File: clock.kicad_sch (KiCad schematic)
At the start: 39 parts, among them P16 SMA, P2 SMA, U19 SI5351C, U30 74LVC1G3157, U31 74LVC1G3157, U33 74HC4051, X1 TCXO

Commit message: Standardize component Value fields
Use Tolerance field instead of expressing tolerance in Value field
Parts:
- C113, C119, C120, C121, C122, C168, C39, C40, C43: value 1uF -> 1 uF
- C155: value 100nF -> 100 nF
- R27, R28: value 1k8 -> 1.8k
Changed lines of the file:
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@@
 			)
 		)
-		(property "Value" "1uF"
+		(property "Value" "1 uF"
 			(at 137.16 182.8799 0)
 			(effects
@@
 			)
 		)
-		(property "Value" "100nF"
+		(property "Value" "100 nF"
 			(at 88.9 99.06 90)
 			(effects
@@
 			)
 		)
-		(property "Value" "1uF"
+		(property "Value" "1 uF"
 			(at 124.46 182.8799 0)
 			(effects
@@
 			)
 		)
-		(property "Value" "1uF"
+		(property "Value" "1 uF"
 			(at 60.96 182.8799 0)
 			(effects
@@
 			)
 		)
-		(property "Value" "1uF"
+		(property "Value" "1 uF"
 			(at 99.06 182.8799 0)
 			(effects
@@
 			)
 		)
-		(property "Value" "1uF"
+		(property "Value" "1 uF"
 			(at 111.76 182.8799 0)
 			(effects
@@
 			)
 		)
-		(property "Value" "1uF"
+		(property "Value" "1 uF"
 			(at 149.86 182.8799 0)
 			(effects
@@
 			)
 		)
-		(property "Value" "1uF"
+		(property "Value" "1 uF"
 			(at 86.36 182.8799 0)
 			(effects
@@
 			)
 		)
-		(property "Value" "1k8"
+		(property "Value" "1.8k"
 			(at 63.5 139.6999 0)
 			(effects
@@
 			)
 		)
-		(property "Value" "1uF"
+		(property "Value" "1 uF"
 			(at 163.83 182.8799 0)
 			(effects
@@
 			)
 		)
-		(property "Value" "1uF"
+		(property "Value" "1 uF"
 			(at 73.66 182.8799 0)
 			(effects
@@
 			)
 		)
-		(property "Value" "1k8"
+		(property "Value" "1.8k"
 			(at 53.34 139.6999 0)
 			(effects

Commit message: Tune mixer output bias and balun
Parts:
- R108, R12, R23, R31, R32, R34, R41, R84: footprint Resistor_SMD:R_0402_1005Metric -> Resistor_SMD:R_0201_0603Metric; Part Number RC0402JR-0733RL -> RC0201JR-0733RL
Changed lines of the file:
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@@
 			)
 		)
-		(property "Footprint" "Resistor_SMD:R_0402_1005Metric"
+		(property "Footprint" "Resistor_SMD:R_0201_0603Metric"
 			(at 152.4 160.02 0)
 			(effects
@@
 			)
 		)
-		(property "Description" "RES 33 OHM 5% 1/16W 0402"
+		(property "Description" "RES 33 OHM 5% 1/20W 0201"
 			(at 152.4 160.02 0)
 			(effects
@@
 			)
 		)
-		(property "Part Number" "RC0402JR-0733RL"
+		(property "Part Number" "RC0201JR-0733RL"
 			(at 152.4 160.02 0)
 			(effects
@@
 			)
 		)
-		(property "Footprint" "Resistor_SMD:R_0402_1005Metric"
+		(property "Footprint" "Resistor_SMD:R_0201_0603Metric"
 			(at 152.4 109.22 0)
 			(effects
@@
 			)
 		)
-		(property "Description" "RES 33 OHM 5% 1/16W 0402"
+		(property "Description" "RES 33 OHM 5% 1/20W 0201"
 			(at 152.4 109.22 0)
 			(effects
@@
 			)
 		)
-		(property "Part Number" "RC0402JR-0733RL"
+		(property "Part Number" "RC0201JR-0733RL"
 			(at 152.4 109.22 0)
 			(effects
@@
 			)
 		)
-		(property "Footprint" "Resistor_SMD:R_0402_1005Metric"
+		(property "Footprint" "Resistor_SMD:R_0201_0603Metric"
 			(at 152.4 88.9 0)
 			(effects
@@
 			)
 		)
-		(property "Description" "RES 33 OHM 5% 1/16W 0402"
+		(property "Description" "RES 33 OHM 5% 1/20W 0201"
 			(at 152.4 88.9 0)
 			(effects
@@
 			)
 		)
-		(property "Part Number" "RC0402JR-0733RL"
+		(property "Part Number" "RC0201JR-0733RL"
 			(at 152.4 88.9 0)
 			(effects
@@
 			)
 		)
-		(property "Footprint" "Resistor_SMD:R_0402_1005Metric"
+		(property "Footprint" "Resistor_SMD:R_0201_0603Metric"
 			(at 152.4 129.54 0)
 			(effects
@@
 			)
 		)
-		(property "Description" "RES 33 OHM 5% 1/16W 0402"
+		(property "Description" "RES 33 OHM 5% 1/20W 0201"
 			(at 152.4 129.54 0)
 			(effects
@@
 			)
 		)
-		(property "Part Number" "RC0402JR-0733RL"
+		(property "Part Number" "RC0201JR-0733RL"
 			(at 152.4 129.54 0)
 			(effects
@@
 			)
 		)
-		(property "Footprint" "Resistor_SMD:R_0402_1005Metric"
+		(property "Footprint" "Resistor_SMD:R_0201_0603Metric"
 			(at 152.4 139.7 0)
 			(effects
@@
 			)
 		)
-		(property "Description" "RES 33 OHM 5% 1/16W 0402"
+		(property "Description" "RES 33 OHM 5% 1/20W 0201"
 			(at 152.4 139.7 0)
 			(effects
@@
 			)
 		)
-		(property "Part Number" "RC0402JR-0733RL"
+		(property "Part Number" "RC0201JR-0733RL"
 			(at 152.4 139.7 0)
 			(effects
@@
 			)
 		)
-		(property "Footprint" "Resistor_SMD:R_0402_1005Metric"
+		(property "Footprint" "Resistor_SMD:R_0201_0603Metric"
 			(at 152.4 99.06 0)
 			(effects
@@
 			)
 		)
-		(property "Description" "RES 33 OHM 5% 1/16W 0402"
+		(property "Description" "RES 33 OHM 5% 1/20W 0201"
 			(at 152.4 99.06 0)
 			(effects
@@
 			)
 		)
-		(property "Part Number" "RC0402JR-0733RL"
+		(property "Part Number" "RC0201JR-0733RL"
 			(at 152.4 99.06 0)
 			(effects
@@
 			)
 		)
-		(property "Footprint" "Resistor_SMD:R_0402_1005Metric"
+		(property "Footprint" "Resistor_SMD:R_0201_0603Metric"
 			(at 232.41 99.06 0)
 			(effects
@@
 			)
 		)
-		(property "Description" "RES 33 OHM 5% 1/16W 0402"
+		(property "Description" "RES 33 OHM 5% 1/20W 0201"
 			(at 232.41 99.06 0)
 			(effects
@@
 			)
 		)
-		(property "Part Number" "RC0402JR-0733RL"
+		(property "Part Number" "RC0201JR-0733RL"
 			(at 232.41 99.06 0)
 			(effects
@@
 			)
 		)
-		(property "Footprint" "Resistor_SMD:R_0402_1005Metric"
+		(property "Footprint" "Resistor_SMD:R_0201_0603Metric"
 			(at 152.4 149.86 0)
 			(effects
@@
 			)
 		)
-		(property "Description" "RES 33 OHM 5% 1/16W 0402"
+		(property "Description" "RES 33 OHM 5% 1/20W 0201"
 			(at 152.4 149.86 0)
 			(effects
@@
 			)
 		)
-		(property "Part Number" "RC0402JR-0733RL"
+		(property "Part Number" "RC0201JR-0733RL"
 			(at 152.4 149.86 0)
 			(effects

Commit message: Connect trigger and PPS I/O signals to MCU
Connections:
- net P6_3 renamed P2_5
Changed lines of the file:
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@@
+		)
+	)
+	(hierarchical_label "P2_5"
+		(shape bidirectional)
+		(at 97.79 69.85 0)
+		(effects
+			(font
+				(size 1.524 1.524)
+			)
+			(justify left)
 		)
 	)
@@
 		)
 	)
-	(hierarchical_label "P6_3"
-		(shape bidirectional)
-		(at 97.79 69.85 0)
-		(effects
-			(font
-				(size 1.524 1.524)
-			)
-			(justify left)
-		)
-	)

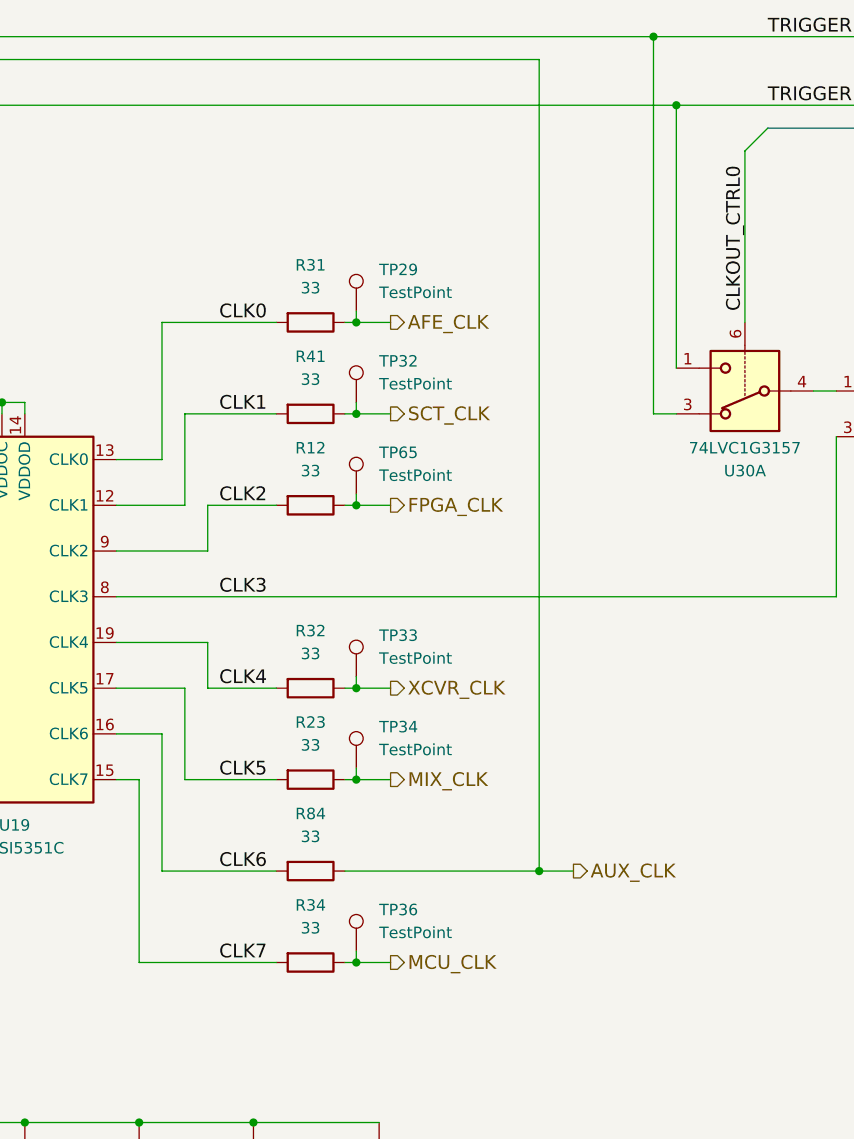
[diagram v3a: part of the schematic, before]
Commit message: Move MCU_CLK from CLK7 to CLK2
- Move FPGA_CLK from CLK2 to CLK1, shared with SCT_CLK
- Add AUX_CLK2 on CLK7
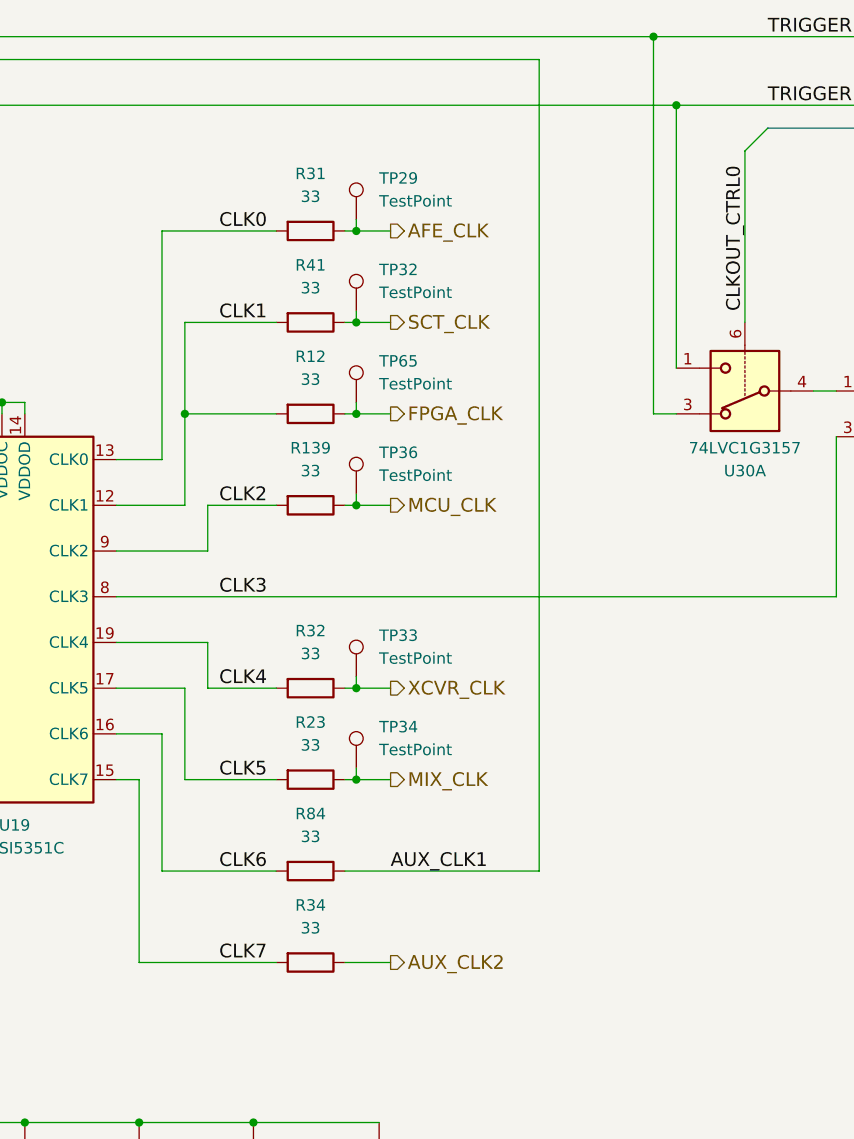
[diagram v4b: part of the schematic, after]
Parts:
- added R139: 33, Resistor_SMD:R_0201_0603Metric, symbol Device:R
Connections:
- net CLK1: now also R12.2
- net CLK2: now also R139.2; no longer R12.2
- net MCU_CLK: now also R139.1; no longer R34.1
- net AUX_CLK renamed AUX_CLK1
- new net AUX_CLK2: R34.1
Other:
- moved on the sheet: R12, R31, R41, TP29, TP32, TP36, TP65

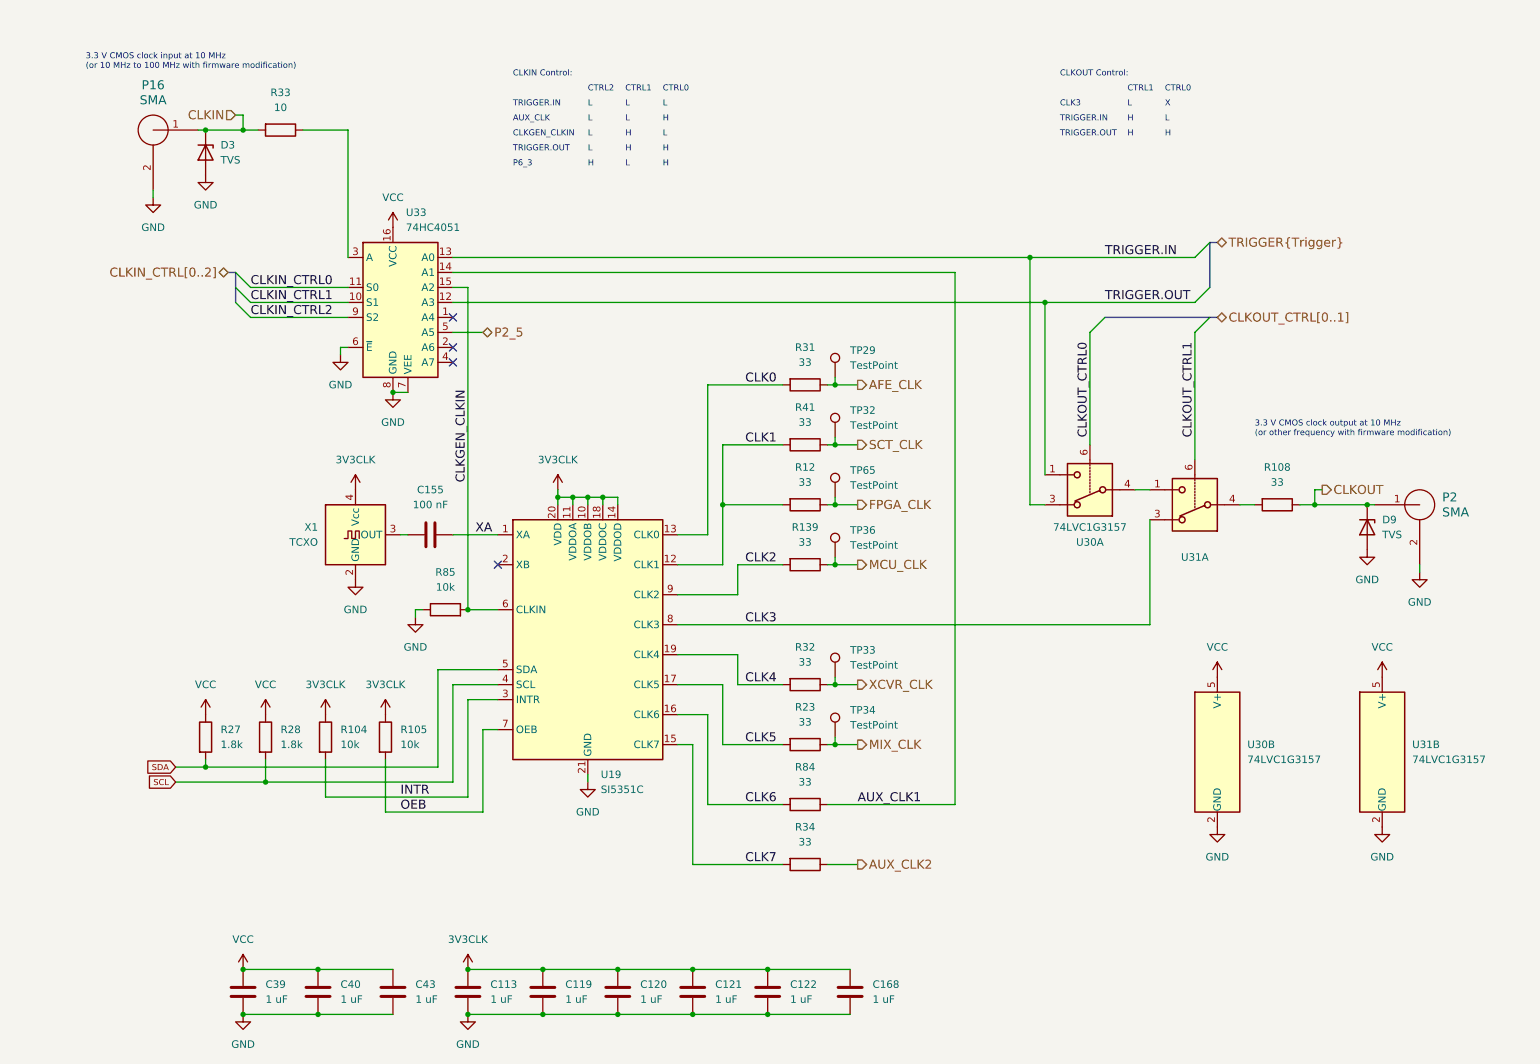
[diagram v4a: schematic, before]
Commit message: Add CLKIN selector switch
- Rename CLKIN SMA connector to P1
- Rename CLKOUT SMA connector to P2
- Allow selection of CLKIN from either P1 or P22
- Add more signals to P1 mux
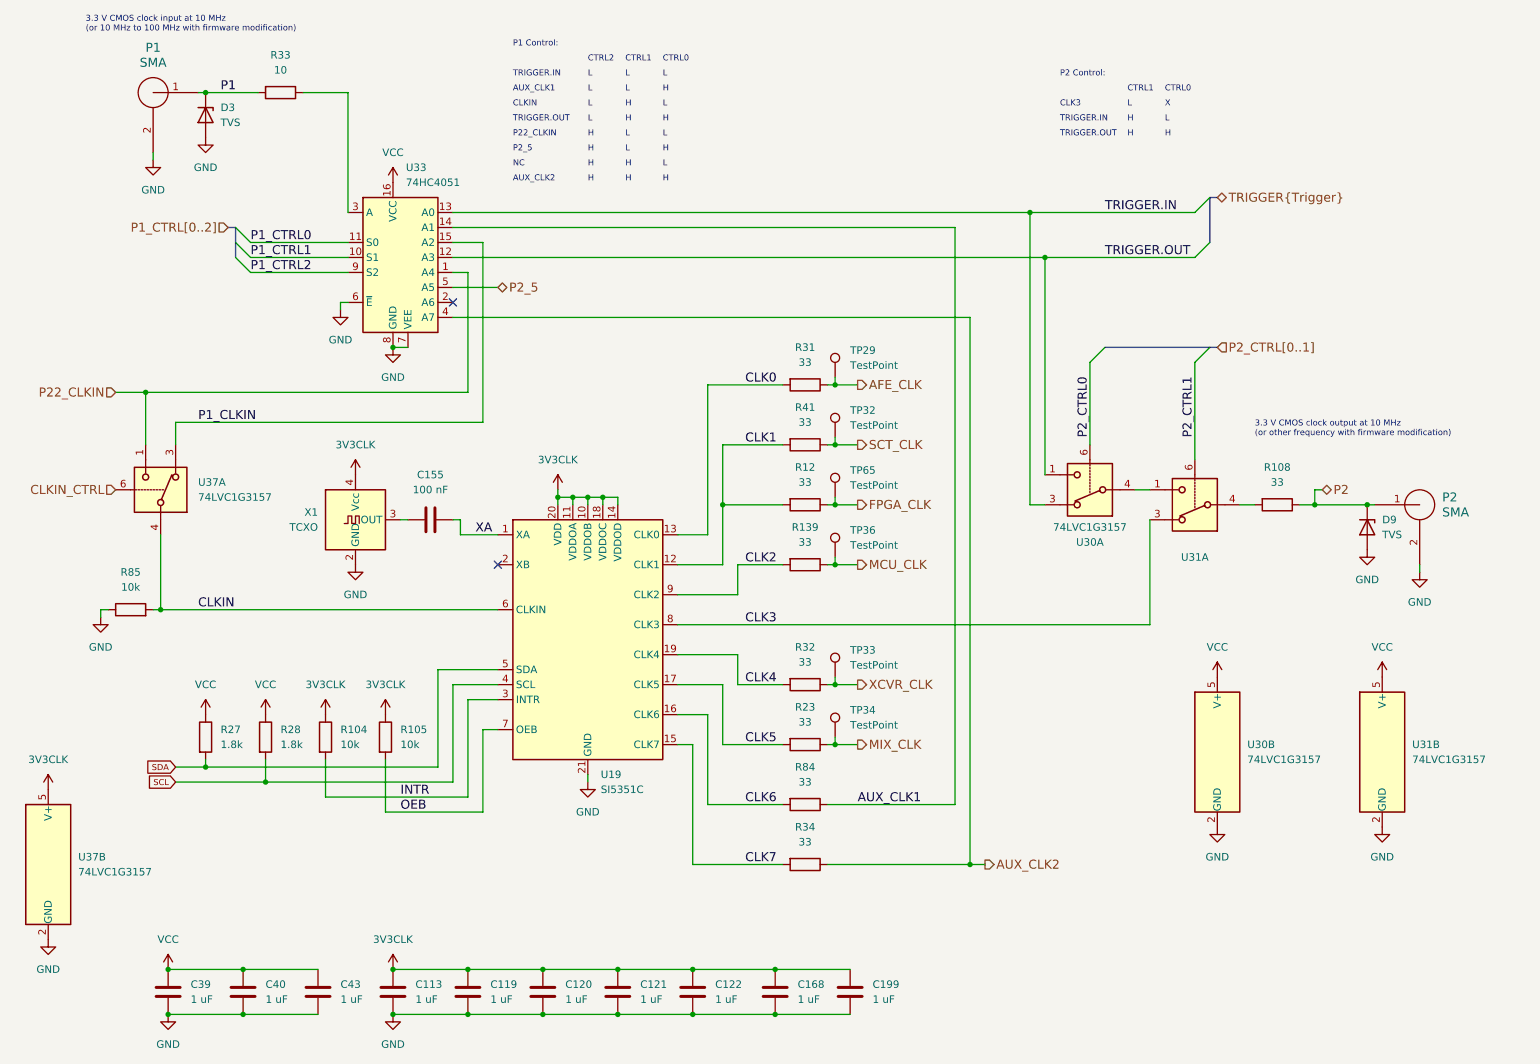
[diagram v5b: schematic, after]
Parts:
- added C199: 1 uF, Capacitor_SMD:C_0402_1005Metric, symbol Device:C
- added U37: 74LVC1G3157, Package_TO_SOT_SMD:SOT-363_SC-70-6, symbol Analog_Switch:NC7SB3157P6X
- renumbered P16 to P1
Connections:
- net 3V3CLK: now also C199.1, U37.5 (V+)
- net AUX_CLK2: now also U33.4 (A7)
- net CLKIN: now also R85.2, U19.6 (CLKIN), U37.4; no longer D3.1 (K), P1.1 (RF), R33.2
- net GND: now also C199.2, U37.2 (GND)
- net P22_CLKIN: now reaches U33.1 (A4)
- net P22_CLKIN: now also U37.1
- removed net CLKGEN_CLKIN: R85.2, U19.6 (CLKIN), U33.15 (A2)
- net CLKIN_CTRL0 renamed P1_CTRL0
- net CLKIN_CTRL1 renamed P1_CTRL1
- net CLKIN_CTRL2 renamed P1_CTRL2
- net CLKOUT renamed P2
- net CLKOUT_CTRL0 renamed P2_CTRL0
- net CLKOUT_CTRL1 renamed P2_CTRL1
- new net CLKIN_CTRL: U37.6
- new net P1: D3.1 (K), P1.1 (RF), R33.2
- new net P1_CLKIN: U33.15 (A2), U37.3
- no-connect marks 4 -> 2
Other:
- note added: "AUX_CLK1"
- note added: "AUX_CLK2"
- note added: "CLKIN"
- note added: "NC"
- note added: "P1 Control:"
- note added: "P2 Control:"
- note added: "P22_CLKIN"
- note added: "P2_5"
- note removed: "AUX_CLK"
- note removed: "CLKGEN_CLKIN"
- note removed: "CLKIN Control:"
- note removed: "CLKOUT Control:"
- note removed: "P6_3"
- moved on the sheet: C113, C119, C120, C121, C122, C155, C168, C39, C40, C43, D3, P1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

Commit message: Make pin 1 marks consistent
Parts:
- X1: footprint Oscillator:Oscillator_SMD_SeikoEpson_TG2520SMN-xxx-xxxxxx-4Pin_2.5x2.0mm -> praline:Oscillator_SMD_SeikoEpson_TG2520SMN-xxx-xxxxxx-4Pin_2.5x2.0mm
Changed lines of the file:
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@@
 			)
 		)
-		(property "Footprint" "Oscillator:Oscillator_SMD_SeikoEpson_TG2520SMN-xxx-xxxxxx-4Pin_2.5x2.0mm"
+		(property "Footprint" "praline:Oscillator_SMD_SeikoEpson_TG2520SMN-xxx-xxxxxx-4Pin_2.5x2.0mm"
 			(at 87.63 110.49 0)
 			(effects
